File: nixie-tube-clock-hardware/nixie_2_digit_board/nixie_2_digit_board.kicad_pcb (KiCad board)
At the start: 2 copper layers, 100 x 47 mm, 93 parts, among them J1 Conn_01x05, J2 Dot Connection, P1 CONN_01X01, P3 CONN_01X01, U1 570Nixie, U10 570Nixie, U11 SN74141-BCD-DEC-DECODE, U2 SN74141-BCD-DEC-DECODE, U3 SN43HC595, U4 570Nixie, U5 SN74141-BCD-DEC-DECODE, U6 Logo, U7 570Nixie, U8 SN74141-BCD-DEC-DECODE, U9 SN43HC595

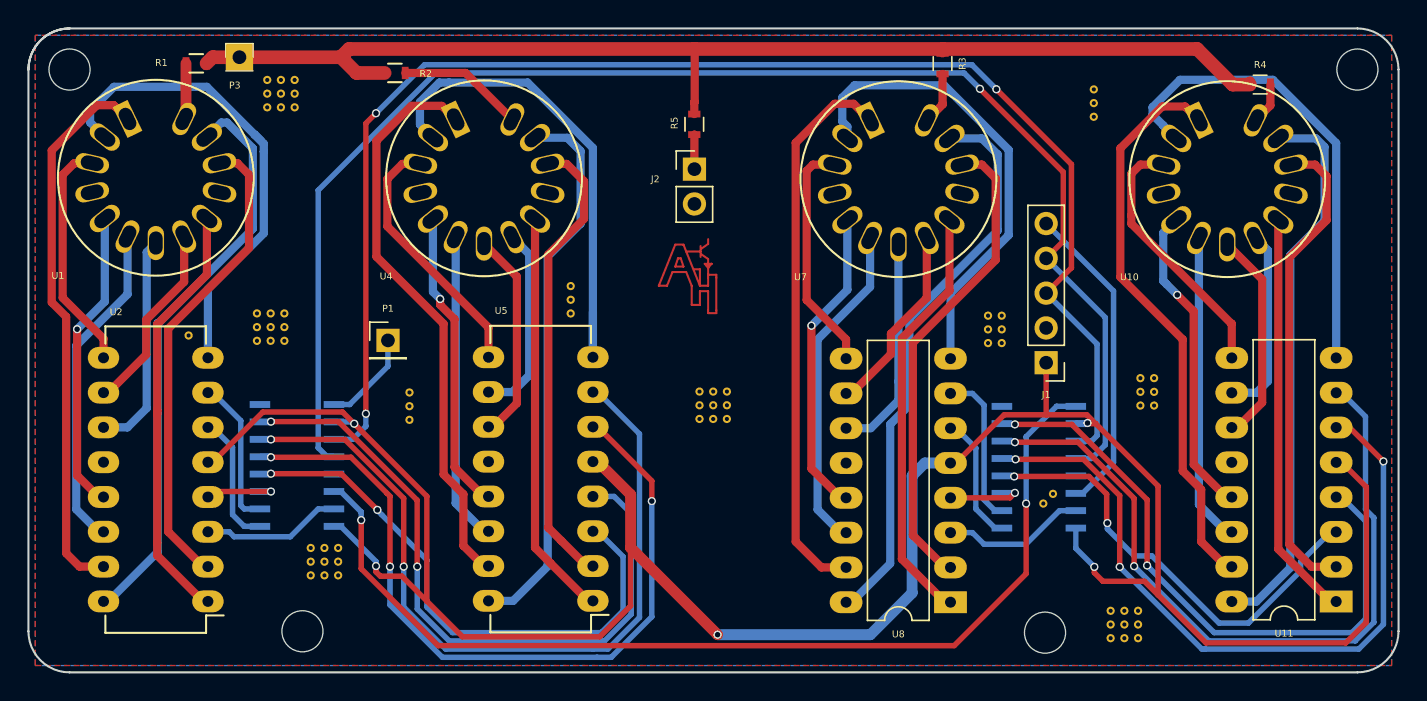
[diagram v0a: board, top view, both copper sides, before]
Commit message: Transistor switch added to dot on nixie board
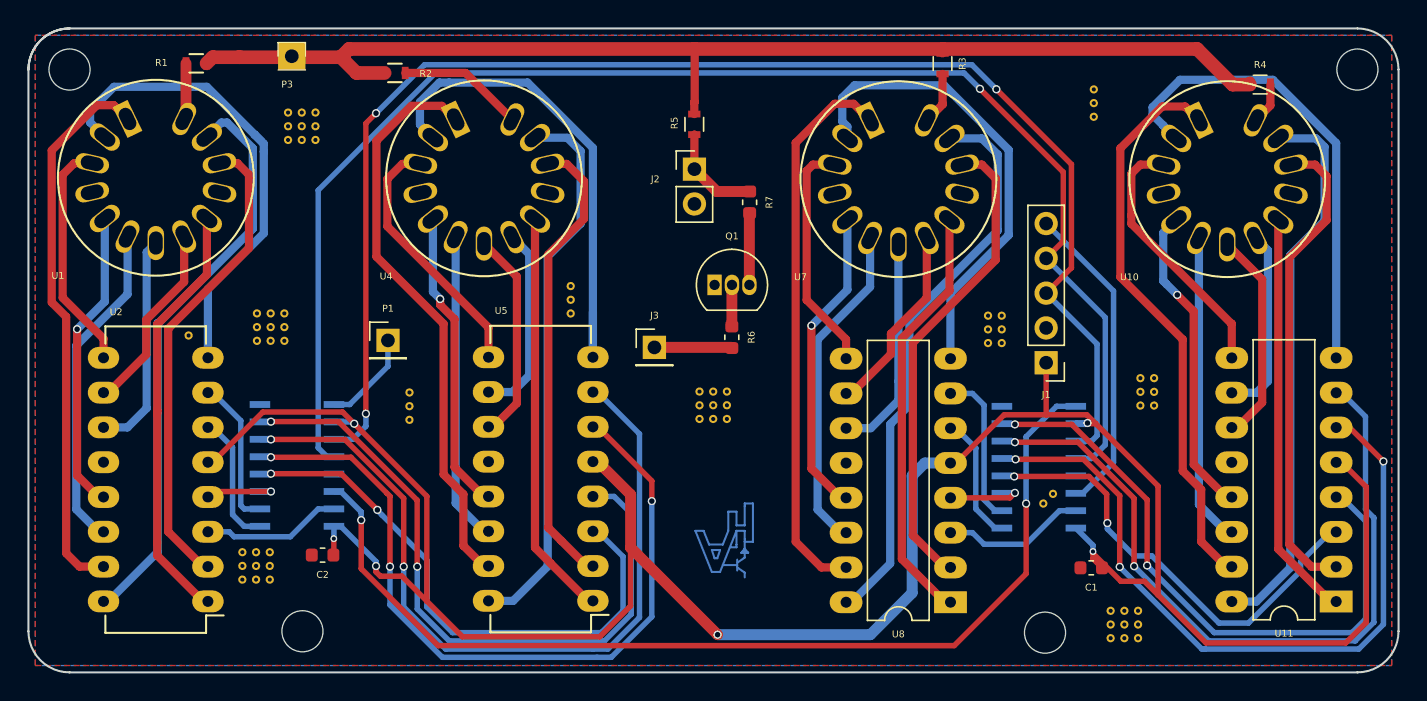
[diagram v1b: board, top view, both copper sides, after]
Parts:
- added C1: 0.1uF, Capacitor_SMD:C_0603_1608Metric, F.Cu at (190.6, 103.4)
- added C2: 0.1uF, Capacitor_SMD:C_0603_1608Metric, F.Cu at (134.5, 102.4)
- added J3: GPIO in for dot, Connector_PinHeader_2.54mm:PinHeader_1x01_P2.54mm_Vertical, F.Cu at (158.7, 87.3)
- added Q1: MPSA42, Package_TO_SOT_THT:TO-92_Inline, F.Cu at (163.1, 82.7)
- added R6: 10K, Resistor_SMD:R_0603_1608Metric, F.Cu at (164.3, 86.5)
- added R7: 15K, Resistor_SMD:R_0603_1608Metric, F.Cu at (165.6, 76.7)
- U6: moved to B.Cu
- moved U6 16.1 mm to (164.9, 99.7)
- moved REF** 5.00 mm to (129.6, 104.2)
- moved REF** 5.00 mm to (128.6, 104.2)
- moved REF** 5.00 mm to (128.6, 103.2)
- moved REF** 5.00 mm to (129.6, 103.2)
- moved REF** 5.00 mm to (130.6, 104.2)
- moved REF** 5.00 mm to (130.6, 103.2)
- moved REF** 5.00 mm to (130.6, 102.2)
- moved REF** 5.00 mm to (129.6, 102.2)
- moved REF** 5.00 mm to (128.6, 102.2)
- moved P3 3.82 mm to (132.2, 66.0)
- moved REF** 2.82 mm to (131.9, 70.1)
- moved REF** 2.82 mm to (132.9, 70.1)
- moved REF** 2.82 mm to (133.9, 70.1)
- moved REF** 2.82 mm to (133.9, 71.1)
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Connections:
- J2 pad 2: GND -> Net-(J2-Pad2)
- R5 pad 1: 180V -> Net-(J2-Pad1)
- R5 pad 2: Net-(J2-Pad1) -> 180V
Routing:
- net DOT_CTRL: track 0.00 -> 5.67 mm
- net Net-(Q1-Pad3): track 0.00 -> 5.25 mm
- net Net-(J2-Pad1): track 2.52 -> 7.23 mm
- net Net-(Q1-Pad2): track 0.00 -> 3.04 mm
- net +5V: track 174.9 -> 177.7 mm, vias 5 -> 6
